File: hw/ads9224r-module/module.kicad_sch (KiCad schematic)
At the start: 11 parts

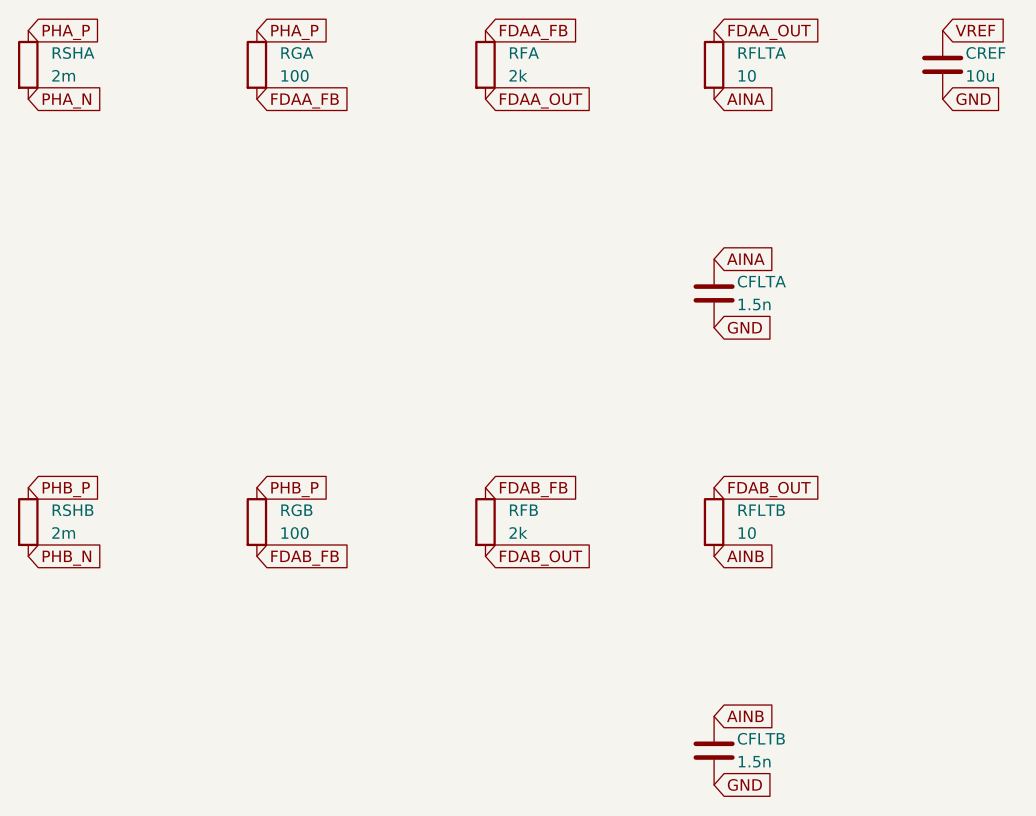
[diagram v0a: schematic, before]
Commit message: Add validation studies and complete README figure index
Add ADS9224R simulation validation, motor-selection, stress-test, and RL experiment reports with generated figures and videos.

Add supporting scripts, tests, SPICE models, motor profiles, and RL environment entry points.

Link every committed figure and gallery from the root README.
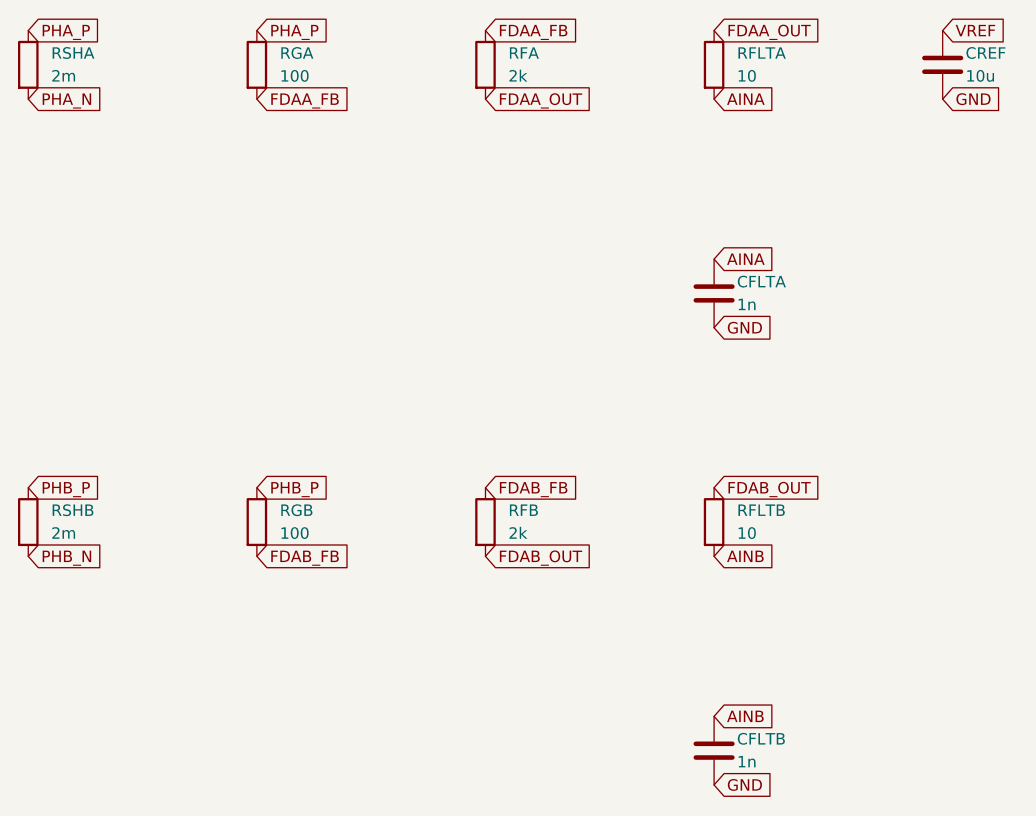
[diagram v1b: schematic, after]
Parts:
- CFLTA, CFLTB: value 1.5n -> 1n
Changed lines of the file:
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@@
     (property "Reference" "CFLTA" (at 129.54 74.92999999999999 0)
       (effects (font (size 1.27 1.27)) (justify left)))
-    (property "Value" "1.5n" (at 129.54 77.46999999999998 0)
+    (property "Value" "1n" (at 129.54 77.46999999999998 0)
       (effects (font (size 1.27 1.27)) (justify left)))
     (property "Footprint" "" (at 127.0 76.19999999999999 0)
@@
     (property "Reference" "CFLTB" (at 129.54 125.73 0)
       (effects (font (size 1.27 1.27)) (justify left)))
-    (property "Value" "1.5n" (at 129.54 128.27 0)
+    (property "Value" "1n" (at 129.54 128.27 0)
       (effects (font (size 1.27 1.27)) (justify left)))
     (property "Footprint" "" (at 127.0 127.0 0)
